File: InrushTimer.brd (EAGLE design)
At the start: 62.2 x 36 mm, 72 parts, among them IC1 TLC272D, IC2 555, IC3 4076N, Q2 TRANSISTOR-FET_2N7002, Q3 TRANSISTOR-FET_2N7002, Q4 TRANSISTOR-FET_2N7002, Q5 TRANSISTOR-FET_2N7002, Q6 DIODES_ZTX451DIODES_ZTX451_0_0, T1 MMBTA05, U1 ROHM_BY_ELEMENT14_BATCH_1_BU4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

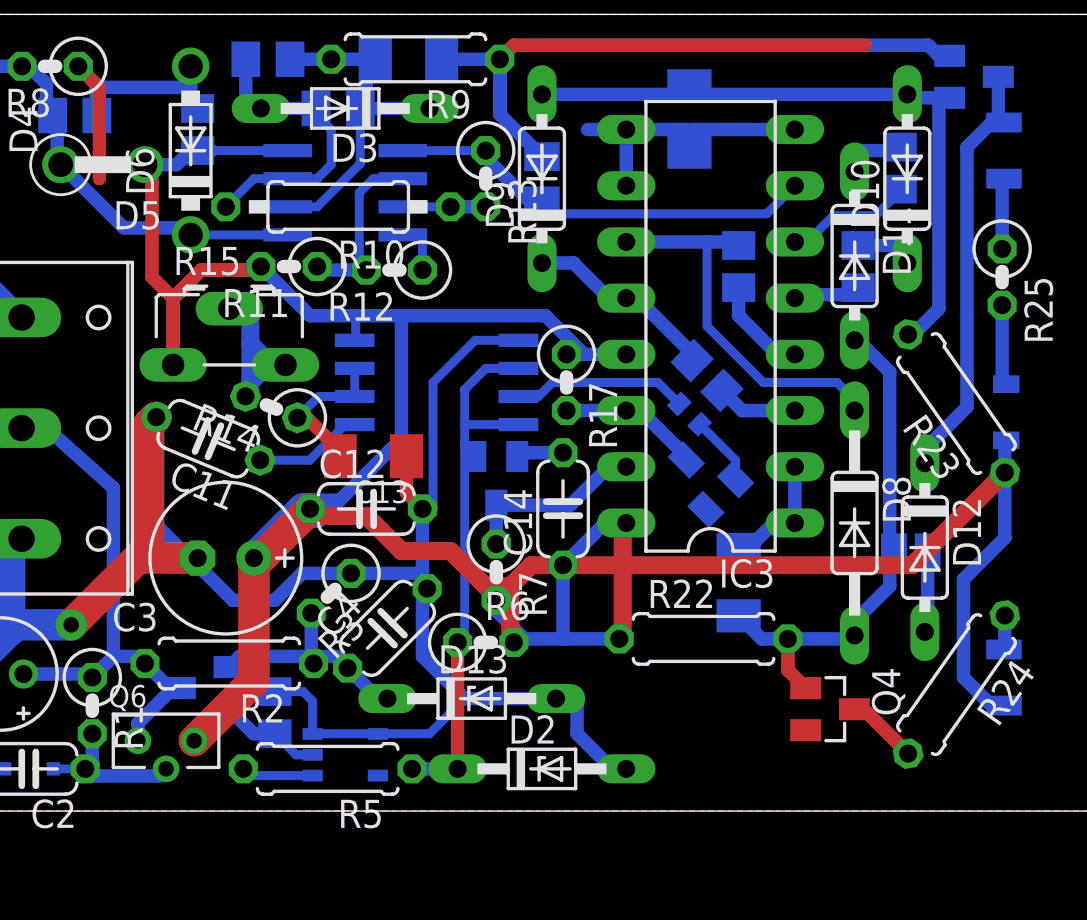
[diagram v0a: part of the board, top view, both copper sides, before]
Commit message: Shifted component to the bottom layer and adjusted some track placements.
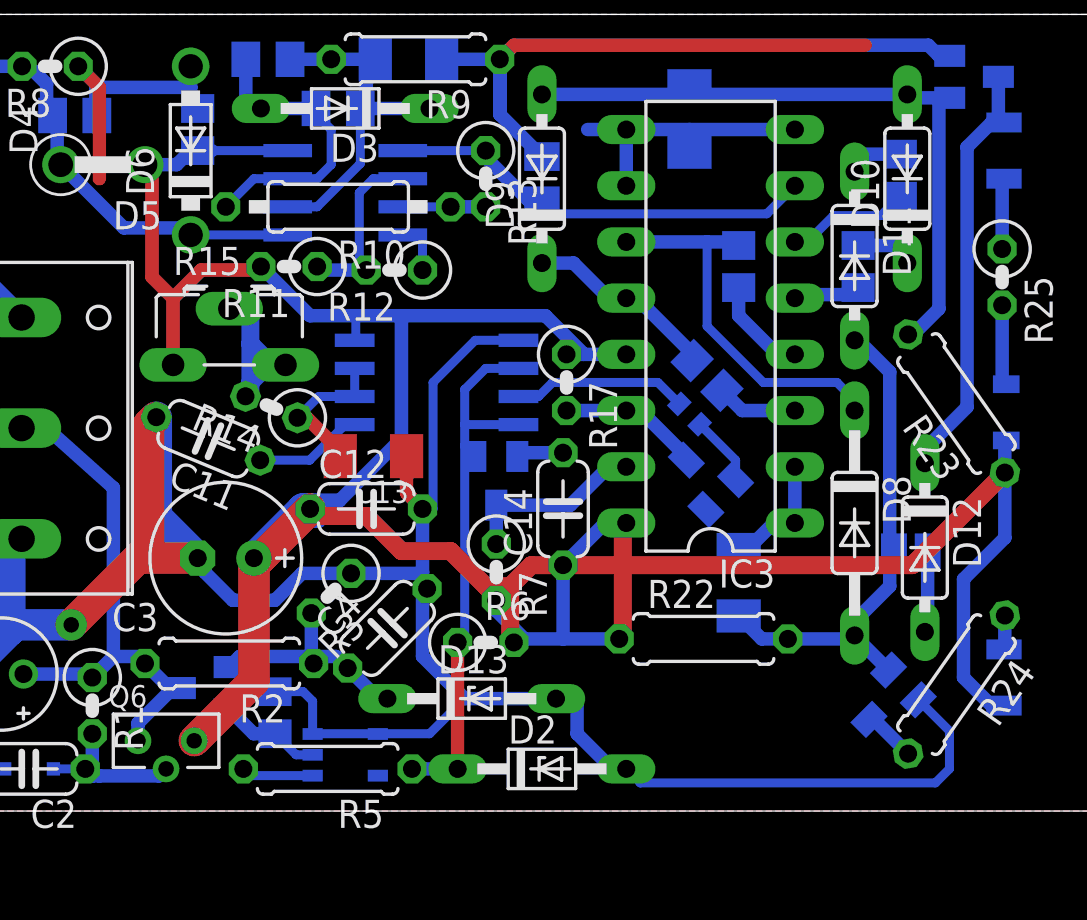
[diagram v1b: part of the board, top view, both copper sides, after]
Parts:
- moved Q4 2.56 mm to (43.2, 4.92), flipped to the bottom, turned to 225 degrees
- moved R21 0.32 mm to (43.8, 28.7)
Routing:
- net ZERO: track 178.5 -> 196.5 mm
- net N$31: track 3.26 -> 2.41 mm
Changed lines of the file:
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@@
 <drawing>
 <settings>
-<setting alwaysvectorfont="no"/>
+<setting alwaysvectorfont="yes"/>
 <setting verticaltext="up"/>
 </settings>
 <grid distance="0.05" unitdist="inch" unit="inch" style="lines" multiple="1" display="no" altdistance="0.0125" altunitdist="inch" altunit="inch"/>
 <layers>
-<layer number="1" name="Top" color="4" fill="1" visible="no" active="yes"/>
+<layer number="1" name="Top" color="4" fill="1" visible="yes" active="yes"/>
 <layer number="2" name="Route2" color="1" fill="3" visible="no" active="no"/>
 <layer number="3" name="Route3" color="4" fill="3" visible="no" active="no"/>
@@
 <attribute name="VALUE" x="18.0975" y="5.08" size="1.27" layer="28" rot="MR270"/>
 </element>
-<element name="R21" library="rcl" package="R0805" value="10K" x="43.815" y="29.05125" rot="MR270"/>
+<element name="R21" library="rcl" package="R0805" value="10K" x="43.815" y="28.73375" rot="MR270"/>
 <element name="R19" library="rcl" package="R0805" value="10K" x="36.5125" y="24.60625" rot="MR270"/>
 <element name="R18" library="rcl" package="R0805" value="10K" x="35.08375" y="19.685" rot="MR225"/>
@@
 <element name="Q2" library="InrushTimer" package="TRANSISTOR-FET_SOT23" value="TRANSISTOR-FET_2N7002" x="25.55875" y="14.9225" rot="MR180"/>
 <element name="Q3" library="InrushTimer" package="TRANSISTOR-FET_SOT23" value="TRANSISTOR-FET_2N7002" x="34.925" y="15.08125" rot="MR315"/>
-<element name="Q4" library="InrushTimer" package="TRANSISTOR-FET_SOT23" value="TRANSISTOR-FET_2N7002" x="40.64" y="4.60375" rot="R270"/>
+<element name="Q4" library="InrushTimer" package="TRANSISTOR-FET_SOT23" value="TRANSISTOR-FET_2N7002" x="43.18" y="4.92125" rot="MR225"/>
 <element name="Q5" library="InrushTimer" package="TRANSISTOR-FET_SOT23" value="TRANSISTOR-FET_2N7002" x="47.14875" y="33.17875" rot="MR90"/>
 <element name="C16" library="rcl" package="C1206K" value="100nF (DNF)" x="34.29" y="31.27375" rot="MR270"/>
@@
 <contactref element="R15" pad="A"/>
 <contactref element="R7" pad="2"/>
-<wire x1="15.08125" y1="24.60625" x2="14.9225" y2="24.60625" width="0.4064" layer="16"/>
 <wire x1="17.145" y1="13.6525" x2="17.4625" y2="13.335" width="0.8128" layer="1"/>
 <wire x1="17.4625" y1="13.335" x2="19.685" y2="13.335" width="0.8128" layer="1"/>
@@
 <wire x1="12.065" y1="11.43" x2="9.525" y2="11.43" width="1.4224" layer="1"/>
 <wire x1="9.525" y1="11.43" x2="9.445625" y2="11.509375" width="1.4224" layer="1"/>
-<wire x1="9.8425" y1="12.7" x2="9.8425" y2="17.447421875" width="1.4224" layer="16"/>
-<wire x1="12.065" y1="11.43" x2="11.1125" y2="11.43" width="1.4224" layer="16"/>
-<wire x1="11.1125" y1="11.43" x2="9.8425" y2="12.7" width="1.4224" layer="16"/>
-<wire x1="9.8425" y1="17.447421875" x2="10.19459375" y2="17.799515625" width="1.4224" layer="16"/>
 <wire x1="9.8425" y1="17.4625" x2="10.16" y2="17.78" width="1.4224" layer="1"/>
 <wire x1="21.3325" y1="26.035" x2="22.225" y2="26.035" width="0.4064" layer="16"/>
@@
 <wire x1="25.7175" y1="33.9725" x2="25.7175" y2="31.48" width="0.6096" layer="16"/>
 <wire x1="25.7175" y1="31.48" x2="27.6225" y2="29.575" width="0.6096" layer="16"/>
+<wire x1="10.19459375" y1="17.799515625" x2="10.19459375" y2="13.30040625" width="1.4224" layer="16"/>
+<wire x1="10.19459375" y1="13.30040625" x2="12.065" y2="11.43" width="1.4224" layer="16"/>
+<wire x1="31.4325" y1="1.905" x2="32.0675" y2="1.27" width="0.4064" layer="16"/>
+<wire x1="32.0675" y1="1.27" x2="45.4025" y2="1.27" width="0.4064" layer="16"/>
+<wire x1="46.0375" y1="3.6193875" x2="44.629571875" y2="5.027315625" width="0.4064" layer="16"/>
+<wire x1="45.4025" y1="1.27" x2="46.0375" y2="1.905" width="0.4064" layer="16"/>
+<wire x1="46.0375" y1="1.905" x2="46.0375" y2="3.6193875" width="0.4064" layer="16"/>
 </signal>
 <signal name="N$9">
@@
 <wire x1="19.16" y1="18.7325" x2="19.16" y2="20.0025" width="0.4064" layer="16"/>
 <contactref element="R14" pad="1"/>
-<wire x1="16.572075" y1="17.842075" x2="16.572075" y2="17.770240625" width="0.4064" layer="16"/>
 <wire x1="18.5025" y1="16.03375" x2="18.5025" y2="16.26375" width="0.6096" layer="1"/>
 <wire x1="18.5025" y1="16.26375" x2="16.996009375" y2="17.770240625" width="0.6096" layer="1"/>
@@
 <wire x1="43.33875" y1="10.16" x2="41.75125" y2="8.5725" width="0.6096" layer="16"/>
 <wire x1="41.75125" y1="8.5725" x2="41.75125" y2="7.9375" width="0.6096" layer="16"/>
-<wire x1="39.54" y1="5.55375" x2="38.735" y2="6.35875" width="0.6096" layer="1"/>
-<wire x1="38.735" y1="6.35875" x2="38.735" y2="7.77875" width="0.6096" layer="1"/>
 <wire x1="43.33875" y1="19.84375" x2="41.91" y2="21.2725" width="0.6096" layer="16"/>
 <wire x1="41.91" y1="21.2725" x2="41.75125" y2="21.2725" width="0.6096" layer="16"/>
+<wire x1="43.28606875" y1="6.37081875" x2="41.75125" y2="7.9056375" width="0.6096" layer="16"/>
+<wire x1="41.75125" y1="7.9056375" x2="41.75125" y2="7.9375" width="0.6096" layer="16"/>
 </signal>
 <signal name="ON_B_SYNC">
@@
 <contactref element="R24" pad="2"/>
 <contactref element="Q4" pad="3"/>
-<wire x1="44.169671875" y1="2.594028125" x2="42.15995" y2="4.60375" width="0.6096" layer="1"/>
-<wire x1="42.15995" y1="4.60375" x2="41.74" y2="4.60375" width="0.6096" layer="1"/>
+<wire x1="44.169671875" y1="2.594028125" x2="42.62026875" y2="4.14343125" width="0.6096" layer="16"/>
+<wire x1="42.62026875" y1="4.14343125" x2="42.402184375" y2="4.14343125" width="0.6096" layer="16"/>
 </signal>
 <signal name="N$4">
@@
 <contactref element="IC3" pad="6"/>
 <contactref element="R21" pad="2"/>
-<wire x1="42.70125" y1="26.908125" x2="40.79875" y2="26.908125" width="0.4064" layer="16"/>
+<wire x1="42.939375" y1="26.908125" x2="40.79875" y2="26.908125" width="0.4064" layer="16"/>
 <wire x1="40.79875" y1="26.908125" x2="39.608125" y2="25.7175" width="0.4064" layer="16"/>
 <wire x1="39.608125" y1="25.7175" x2="39.0525" y2="25.7175" width="0.4064" layer="16"/>
-<wire x1="42.70125" y1="26.908125" x2="43.815" y2="28.021875" width="0.4064" layer="16"/>
-<wire x1="43.815" y1="28.021875" x2="43.815" y2="28.10125" width="0.4064" layer="16"/>
+<wire x1="42.939375" y1="26.908125" x2="43.815" y2="27.78375" width="0.4064" layer="16"/>
 </signal>
 <signal name="N$25">
@@
 <contactref element="D11" pad="C"/>
 <contactref element="R21" pad="1"/>
-<wire x1="43.815" y1="30.00125" x2="43.65875" y2="29.845" width="0.6096" layer="16"/>
-<wire x1="43.65875" y1="29.845" x2="41.75125" y2="29.845" width="0.6096" layer="16"/>
-<wire x1="41.75125" y1="29.845" x2="41.75125" y2="28.8925" width="0.6096" layer="16"/>
+<wire x1="43.815" y1="29.68375" x2="41.75125" y2="29.68375" width="0.6096" layer="16"/>
+<wire x1="41.75125" y1="29.68375" x2="41.75125" y2="28.8925" width="0.6096" layer="16"/>
 </signal>
 <signal name="N$20">

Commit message: Track and component positions.
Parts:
- moved D9 0.64 mm to (28.3, 28.6)
- moved R16 0.45 mm to (34.6, 17.6)
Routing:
- net ZERO: track 196.5 -> 185.4 mm
- net ON_B_SYNC: track 30.3 -> 29.6 mm
- net N$16: track 8.80 -> 8.17 mm
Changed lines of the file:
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@@
 <element name="R14" library="rcl" package="0207/2V" value="100K" x="15.39875" y="18.25625" rot="R157.5"/>
 <element name="C13" library="rcl" package="C1206K" value="2.2uF" x="20.0025" y="16.03375" rot="R180"/>
-<element name="R16" library="rcl" package="R0402" value="1K" x="34.29" y="17.93875" rot="MR45"/>
+<element name="R16" library="rcl" package="R0402" value="1K" x="34.6075" y="17.62125" rot="MR45"/>
 <element name="R17" library="rcl" package="0207/2V" value="51K" x="28.73375" y="19.3675" rot="R270"/>
 <element name="C12" library="rcl" package="C050-024X044" value="100nF" x="19.685" y="13.6525"/>
@@
 <element name="R22" library="rcl" package="0207/7" value="200K" x="34.925" y="7.77875"/>
 <element name="R23" library="rcl" package="0207/7" value="200K" x="46.355" y="18.415" rot="R125"/>
-<element name="D9" library="diode" package="DO35-7" value="1N4148DO35-7" x="27.6225" y="28.575" rot="R90"/>
+<element name="D9" library="diode" package="DO35-7" value="1N4148DO35-7" x="28.2575" y="28.575" rot="R90"/>
 <element name="SJ1" library="jumper" package="SJ" value="" x="44.29125" y="11.7475" rot="MR180"/>
 <element name="C14" library="rcl" package="C050-024X044" value="100nF" x="28.575" y="13.6525" rot="R90"/>
@@
 <contactref element="R1" pad="1"/>
 <contactref element="R2" pad="2"/>
-<wire x1="4.191" y1="6.19125" x2="7.46125" y2="6.19125" width="0.6096" layer="16"/>
-<wire x1="4.1075" y1="17.30375" x2="5.23875" y2="17.30375" width="0.6096" layer="16"/>
-<wire x1="8.255" y1="14.605" x2="8.255" y2="6.985" width="0.6096" layer="16"/>
-<wire x1="8.255" y1="14.605" x2="5.23875" y2="17.30375" width="0.6096" layer="16"/>
-<wire x1="7.46125" y1="6.19125" x2="8.255" y2="6.985" width="0.6096" layer="16"/>
-<wire x1="8.255" y1="6.985" x2="9.68375" y2="6.985" width="0.6096" layer="16"/>
-<wire x1="9.68375" y1="6.985" x2="9.68375" y2="6.6675" width="0.6096" layer="16"/>
 <wire x1="11.2825" y1="5.55625" x2="10.795" y2="5.55625" width="0.6096" layer="16"/>
 <wire x1="10.795" y1="5.55625" x2="10.715625" y2="5.635625" width="0.6096" layer="16"/>
@@
 <wire x1="9.36625" y1="3.96875" x2="10.715625" y2="5.318125" width="0.6096" layer="16"/>
 <wire x1="10.715625" y1="5.318125" x2="10.715625" y2="5.635625" width="0.6096" layer="16"/>
-<wire x1="7.46125" y1="6.19125" x2="7.3025" y2="6.0325" width="0.6096" layer="16"/>
+<wire x1="4.1075" y1="17.30375" x2="4.92125" y2="17.30375" width="1.4224" layer="16"/>
+<wire x1="4.92125" y1="17.30375" x2="8.5725" y2="13.6525" width="1.4224" layer="16"/>
+<wire x1="8.5725" y1="13.6525" x2="8.5725" y2="6.6675" width="1.4224" layer="16"/>
+<wire x1="4.191" y1="6.19125" x2="7.46125" y2="6.19125" width="1.4224" layer="16"/>
+<wire x1="7.62" y1="6.19125" x2="7.77875" y2="6.19125" width="1.4224" layer="16"/>
+<wire x1="7.77875" y1="6.19125" x2="8.255" y2="6.6675" width="1.4224" layer="16"/>
+<wire x1="8.5725" y1="6.6675" x2="9.68375" y2="6.6675" width="1.4224" layer="16"/>
+<wire x1="8.255" y1="6.6675" x2="8.5725" y2="6.6675" width="1.4224" layer="16"/>
+<wire x1="7.3025" y1="6.0325" x2="7.46125" y2="6.19125" width="1.4224" layer="16"/>
+<wire x1="7.46125" y1="6.19125" x2="7.62" y2="6.19125" width="1.4224" layer="16"/>
 </signal>
 <signal name="N$8">
@@
 <via x="6.35" y="8.41375" extent="1-16" drill="0.7" diameter="1.4224" shape="octagon"/>
 <wire x1="3.345" y1="1.905" x2="1.905" y2="1.905" width="0.4064" layer="16"/>
-<wire x1="1.905" y1="1.905" x2="1.905" y2="6.50875" width="1.4224" layer="16"/>
-<wire x1="3.81" y1="8.41375" x2="3.571875" y2="8.175625" width="1.4224" layer="16"/>
-<wire x1="3.571875" y1="8.175625" x2="1.984375" y2="6.588125" width="1.4224" layer="16"/>
-<wire x1="1.984375" y1="6.588125" x2="1.905" y2="6.50875" width="1.4224" layer="16"/>
-<wire x1="2.159" y1="6.19125" x2="2.159" y2="6.4135" width="1.4224" layer="16"/>
-<wire x1="2.159" y1="6.4135" x2="1.984375" y2="6.588125" width="1.4224" layer="16"/>
-<wire x1="4.1075" y1="12.30375" x2="3.571875" y2="12.30375" width="1.4224" layer="16"/>
-<wire x1="3.571875" y1="12.30375" x2="3.571875" y2="8.175625" width="1.4224" layer="16"/>
-<wire x1="3.81" y1="8.41375" x2="6.35" y2="8.41375" width="1.4224" layer="16"/>
 <contactref element="R3" pad="1"/>
 <wire x1="30.7975" y1="1.905" x2="31.4325" y2="1.905" width="0.6096" layer="16"/>
@@
 <wire x1="25.7175" y1="33.9725" x2="25.7175" y2="31.48" width="0.6096" layer="16"/>
 <wire x1="25.7175" y1="31.48" x2="27.6225" y2="29.575" width="0.6096" layer="16"/>
-<wire x1="10.19459375" y1="17.799515625" x2="10.19459375" y2="13.30040625" width="1.4224" layer="16"/>
-<wire x1="10.19459375" y1="13.30040625" x2="12.065" y2="11.43" width="1.4224" layer="16"/>
 <wire x1="31.4325" y1="1.905" x2="32.0675" y2="1.27" width="0.4064" layer="16"/>
 <wire x1="32.0675" y1="1.27" x2="45.4025" y2="1.27" width="0.4064" layer="16"/>
@@
 <wire x1="45.4025" y1="1.27" x2="46.0375" y2="1.905" width="0.4064" layer="16"/>
 <wire x1="46.0375" y1="1.905" x2="46.0375" y2="3.6193875" width="0.4064" layer="16"/>
+<wire x1="10.19459375" y1="17.799515625" x2="12.065" y2="15.929109375" width="1.4224" layer="16"/>
+<wire x1="12.065" y1="15.929109375" x2="12.065" y2="11.43" width="1.4224" layer="16"/>
+<wire x1="2.159" y1="6.35" x2="2.159" y2="8.255" width="1.4224" layer="16"/>
+<wire x1="2.159" y1="4.28625" x2="2.159" y2="6.19125" width="1.4224" layer="16"/>
 </signal>
 <signal name="N$9">
@@
 <contactref element="Q3" pad="1"/>
 <wire x1="36.374571875" y1="14.97518125" x2="36.374571875" y2="15.854178125" width="0.4064" layer="16"/>
-<wire x1="36.374571875" y1="15.854178125" x2="34.749621875" y2="17.479128125" width="0.4064" layer="16"/>
+<wire x1="36.374571875" y1="15.854178125" x2="35.067121875" y2="17.161628125" width="0.4064" layer="16"/>
 </signal>
 <signal name="N$40">
@@
 <wire x1="26.56" y1="18.7325" x2="27.46375" y2="18.7325" width="0.4064" layer="16"/>
 <wire x1="27.46375" y1="18.7325" x2="28.09875" y2="19.3675" width="0.4064" layer="16"/>
+<wire x1="34.14788125" y1="18.08086875" x2="32.86125" y2="19.3675" width="0.4064" layer="16"/>
 <wire x1="32.86125" y1="19.3675" x2="28.09875" y2="19.3675" width="0.4064" layer="16"/>
-<wire x1="33.83038125" y1="18.39836875" x2="32.86125" y2="19.3675" width="0.4064" layer="16"/>
 </signal>
 <signal name="N$1">
@@
 <wire x1="45.56125" y1="32.22875" x2="44.28875" y2="32.22875" width="0.6096" layer="16"/>
 <wire x1="45.56125" y1="22.70125" x2="45.56125" y2="32.22875" width="0.6096" layer="16"/>
-<wire x1="27.6225" y1="32.385" x2="34.29" y2="32.385" width="0.6096" layer="16"/>
 <wire x1="34.29" y1="32.385" x2="44.1325" y2="32.385" width="0.6096" layer="16"/>
 <wire x1="34.29" y1="32.77375" x2="34.29" y2="32.385" width="0.6096" layer="16"/>
@@
 <wire x1="44.39596875" y1="21.53596875" x2="44.169671875" y2="21.53596875" width="0.6096" layer="16"/>
 <wire x1="44.28875" y1="32.22875" x2="44.1325" y2="32.385" width="0.6096" layer="16"/>
+<wire x1="34.29" y1="32.385" x2="28.2575" y2="32.385" width="0.6096" layer="16"/>
 </signal>
 <signal name="N$6">
@@
 <contactref element="IC3" pad="12"/>
 <contactref element="D9" pad="C"/>
-<wire x1="27.6225" y1="24.765" x2="29.05125" y2="24.765" width="0.6096" layer="16"/>
 <wire x1="29.05125" y1="24.765" x2="30.63875" y2="23.1775" width="0.6096" layer="16"/>
 <wire x1="30.63875" y1="23.1775" x2="31.4325" y2="23.1775" width="0.6096" layer="16"/>
@@
 <wire x1="34.412" y1="20.67425" x2="31.90875" y2="23.1775" width="0.6096" layer="16"/>
 <wire x1="31.90875" y1="23.1775" x2="31.4325" y2="23.1775" width="0.6096" layer="16"/>
+<wire x1="29.05125" y1="24.765" x2="28.2575" y2="24.765" width="0.6096" layer="16"/>
 </signal>
 <signal name="N$22">
